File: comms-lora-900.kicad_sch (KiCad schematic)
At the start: 3 parts, among them J3 Conn_Coaxial_Small, U3 RFM95W-915S2

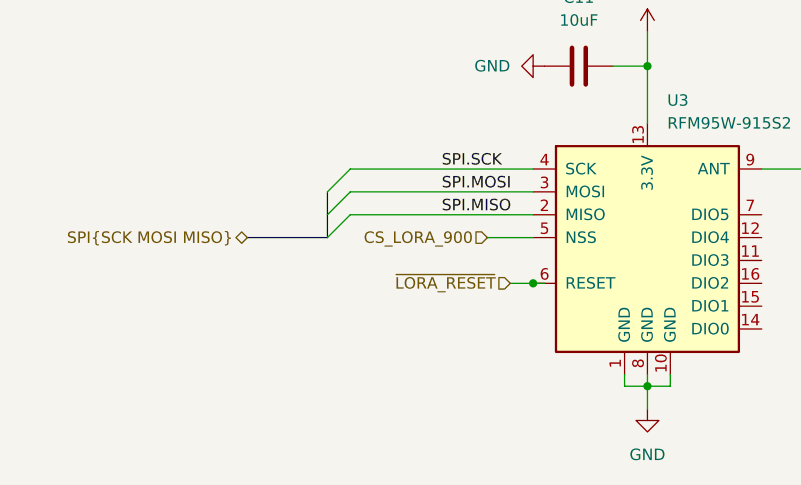
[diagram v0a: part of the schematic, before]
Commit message: Adding symbols information
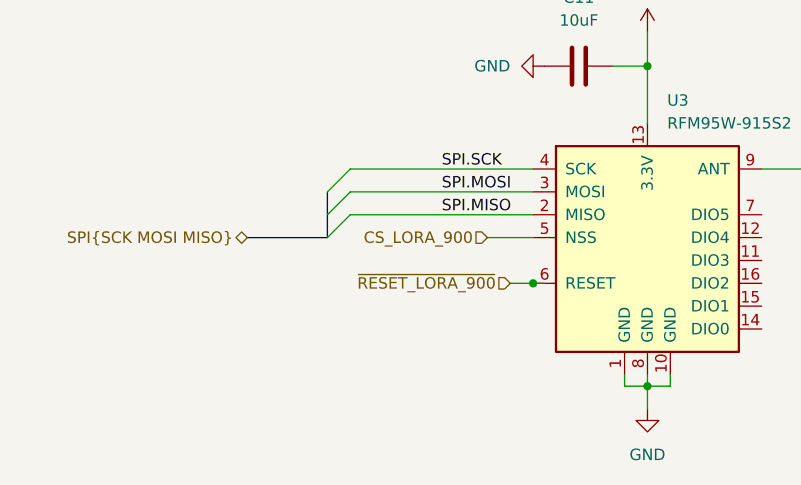
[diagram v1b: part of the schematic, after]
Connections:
- net ~{LORA_RESET} renamed ~{RESET_LORA_900}
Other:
- company: (none) -> catbranchman
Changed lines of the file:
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@@
 	(generator_version "8.0")
 	(paper "A4")
+	(title_block
+		(company "catbranchman")
+		(comment 1 "Electrical Engineering Department")
+		(comment 2 "EE 156 / Stanford University")
+		(comment 3 "Flight Club, W6YX, Endurance")
+	)
 	(junction
 		(at 144.78 114.3)
@@
 		)
 	)
-	(hierarchical_label "~{LORA_RESET}"
+	(hierarchical_label "~{RESET_LORA_900}"
 		(shape input)
 		(at 129.54 102.87 180)
@@
 		)
 		(instances
-			(project ""
+			(project "roamer"
 				(path "/1c59de6a-87fe-4223-8898-4b0383164a31/74b4b058-6b85-4b9e-95dc-72d767f949d9"
 					(reference "J3")
@@
 		)
 		(instances
-			(project ""
+			(project "roamer"
 				(path "/1c59de6a-87fe-4223-8898-4b0383164a31/74b4b058-6b85-4b9e-95dc-72d767f949d9"
 					(reference "C11")

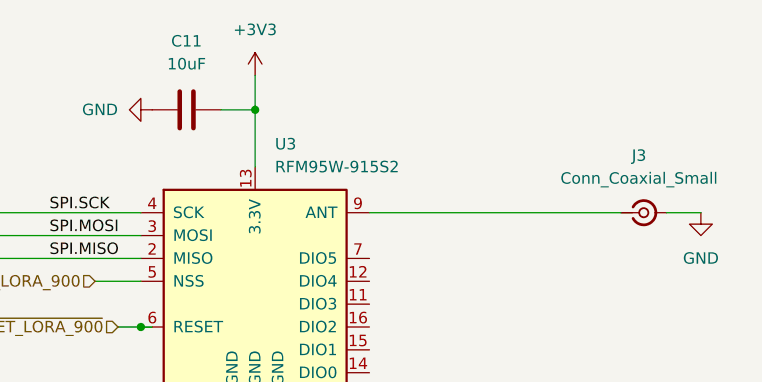
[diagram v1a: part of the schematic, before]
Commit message: Adding rest of schematic
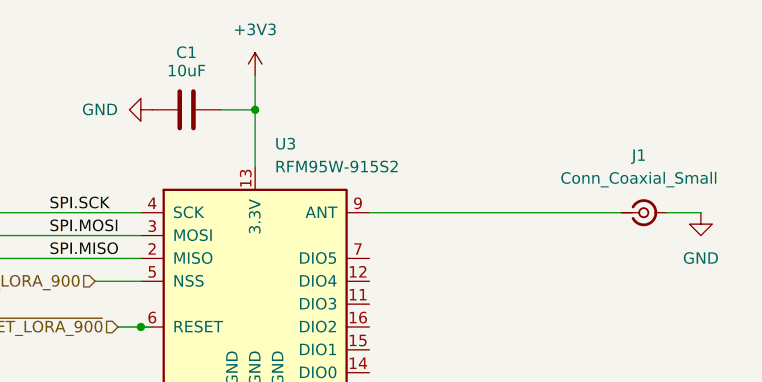
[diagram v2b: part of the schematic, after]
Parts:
- removed C11: 10uF, symbol Device:C
- removed J3: Conn_Coaxial_Small, symbol Connector:Conn_Coaxial_Small
- added C1: 10uF, Inductor_SMD:L_0805_2012Metric, symbol Device:C
- added J1: Conn_Coaxial_Small, Connector_Coaxial:U.FL_Molex_MCRF_73412-0110_Vertical, symbol Connector:Conn_Coaxial_Small
- U3: footprint (none) -> RF_Module:HOPERF_RFM9XW_SMD; Mfr (none) -> Adafruit; Mfr P/N (none) -> 3072; Supplier_1 (none) -> Supplier_1 P/N 0 0 Center Center 0 0; Supplier_1 P/N (none) -> 3072; Supplier_1 Price @ Qty (none) -> $15.96; Supplier_1 Unit Price (none) -> $19.95
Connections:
- net +3V3: now also C1.2
- net GND: now also C1.1, J1.2 (Ext)
- net at U3.9 (ANT): now also J1.1 (In)

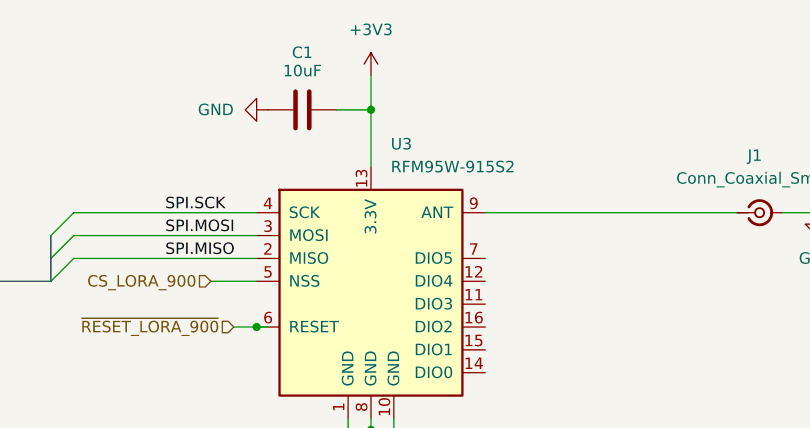
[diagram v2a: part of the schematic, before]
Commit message: Fixing footprint imports
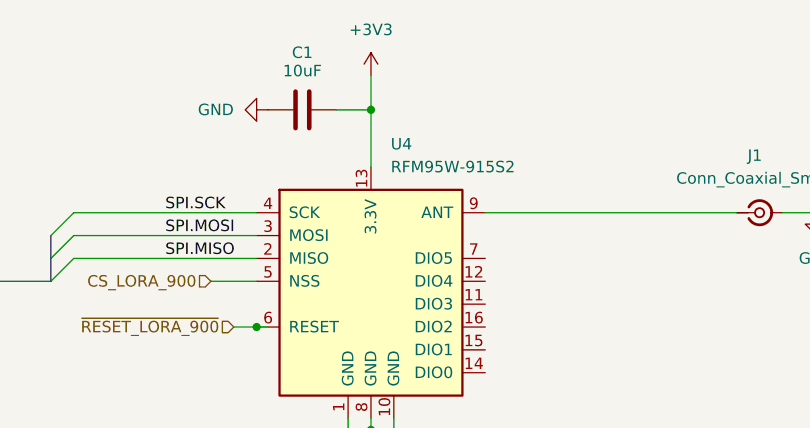
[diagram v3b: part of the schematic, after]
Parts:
- renumbered U3 to U4
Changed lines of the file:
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@@
 		(dnp no)
 		(fields_autoplaced yes)
-		(property "Reference" "U3"
+		(property "Reference" "U4"
 			(at 146.9741 82.55 0)
 			(effects
@@
 			(project "roamer"
 				(path "/1c59de6a-87fe-4223-8898-4b0383164a31/74b4b058-6b85-4b9e-95dc-72d767f949d9"
-					(reference "U3")
+					(reference "U4")
 					(unit 1)
 				)

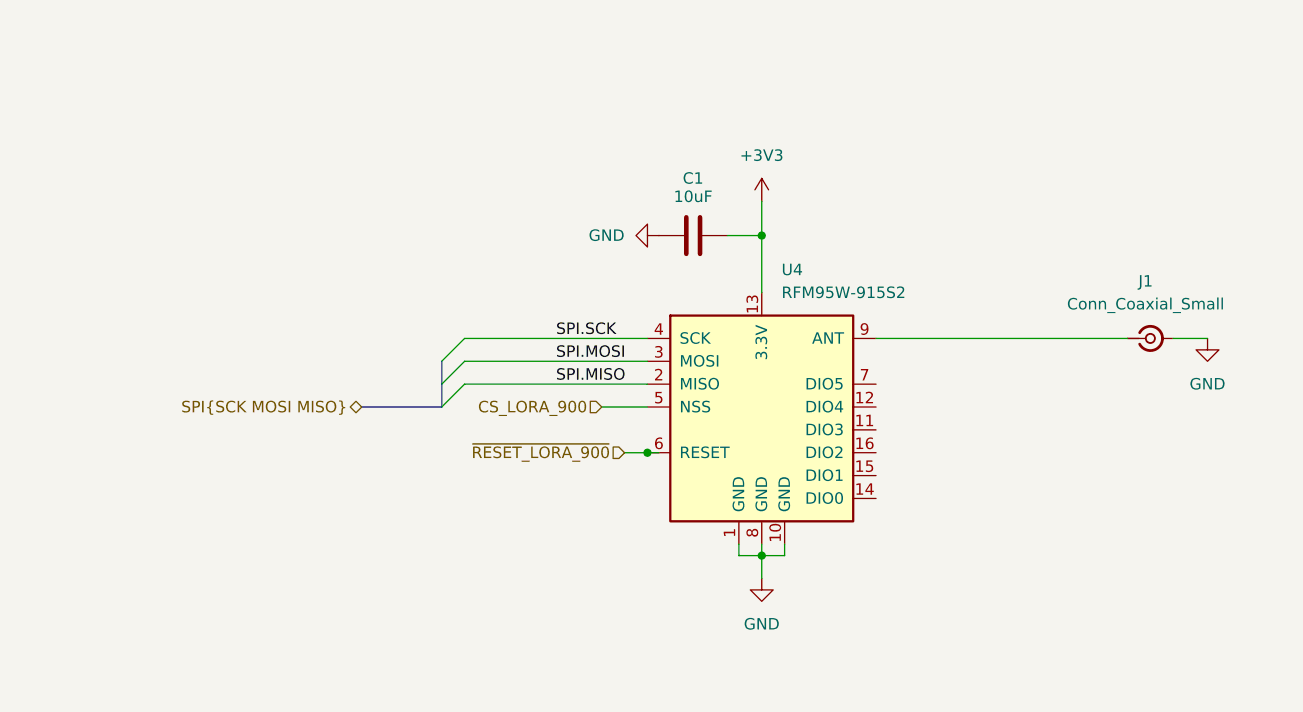
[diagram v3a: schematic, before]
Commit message: Spamming 0 ohm resistors
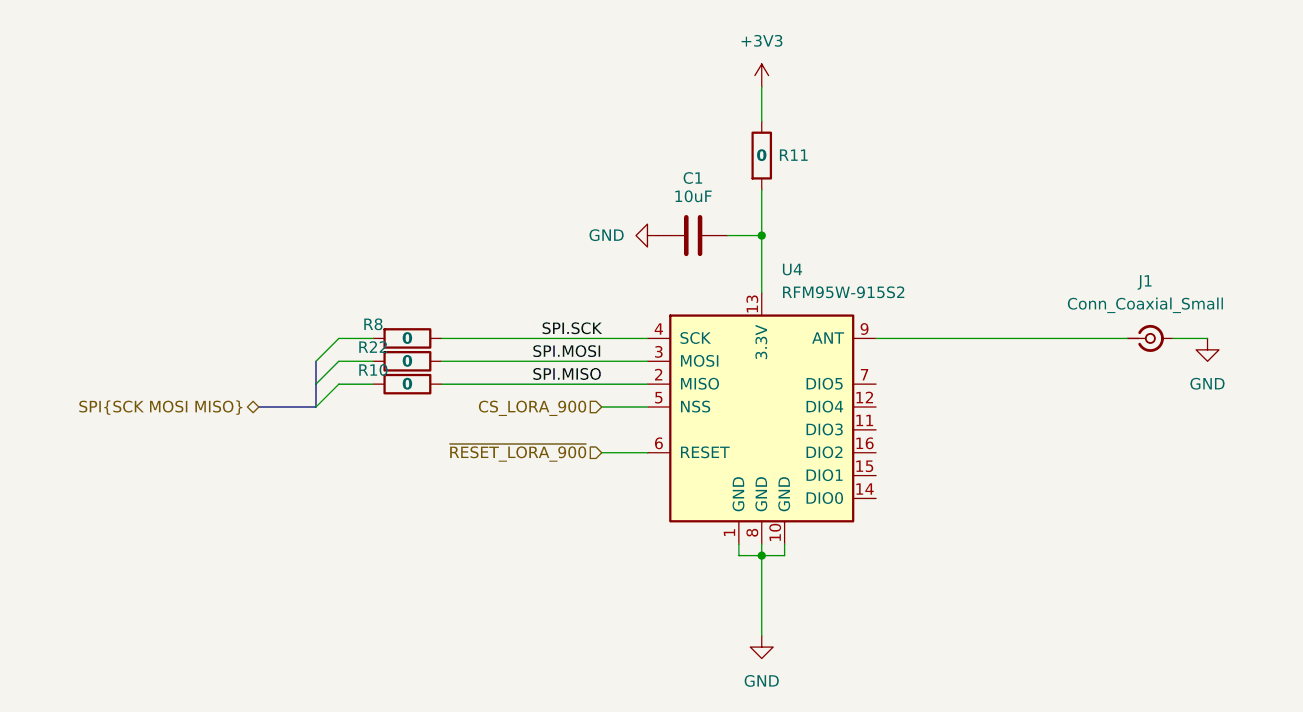
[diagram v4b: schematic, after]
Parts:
- added R10, R11, R22, R8: 0, Resistor_SMD:R_0603_1608Metric, symbol Device:R
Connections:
- net +3V3: now also R11.1; no longer C1.2, U4.13 (3.3V)
- net SPI.MISO: now also R10.1
- net SPI.MOSI: now also R22.1
- net SPI.SCK: now also R8.1
- new net: C1.2, R11.2, U4.13 (3.3V)
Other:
- title: (none) -> Comms - LoRa 900

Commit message: Adding more 0 ohm resistors and pullups for I2C lines
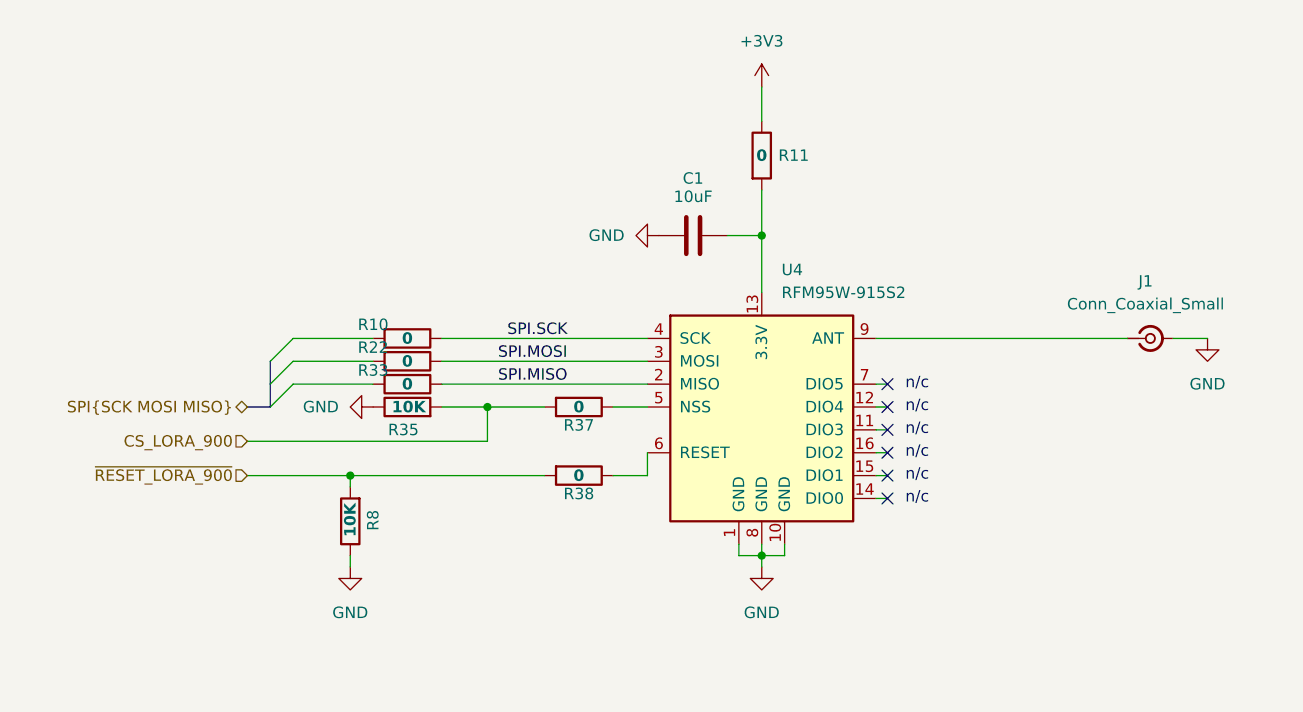
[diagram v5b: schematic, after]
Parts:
- added R33, R37, R38: 0, Resistor_SMD:R_0603_1608Metric, symbol Device:R
- added R35: 10K, Resistor_SMD:R_0603_1608Metric, symbol Device:R
- R8: value 0 -> 10K; Mfr YAGEO -> Stackpole Electronics Inc; Mfr P/N RC0603JR-070RL -> RNCP0603FTD10K0; Supplier_1 P/N 311-0.0GRCT-ND -> RNCP0603FTD10K0CT-ND; Supplier_1 Price @ Qty $0.00304 -> 0.0170; Supplier_1 Unit Price $0.10000 -> 0.10
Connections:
- net CS_LORA_900: now also R35.2, R37.2; no longer U4.5 (NSS)
- net GND: now also R8.1, R35.1
- net SPI.MISO: now also R33.1; no longer R10.1
- net SPI.SCK: now also R10.1; no longer R8.1
- net ~{RESET_LORA_900}: now also R8.2, R38.2; no longer U4.6 (RESET)
- new net: R38.1, U4.6 (RESET)
- new net: R37.1, U4.5 (NSS)
- no-connect marks 0 -> 6
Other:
- note added: "n/c"

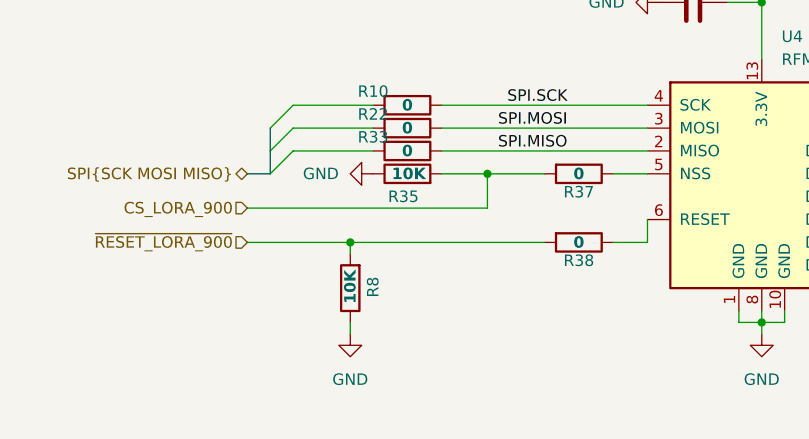
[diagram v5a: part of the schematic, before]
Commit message: Adding testpoints to I2C, SPI, and signals
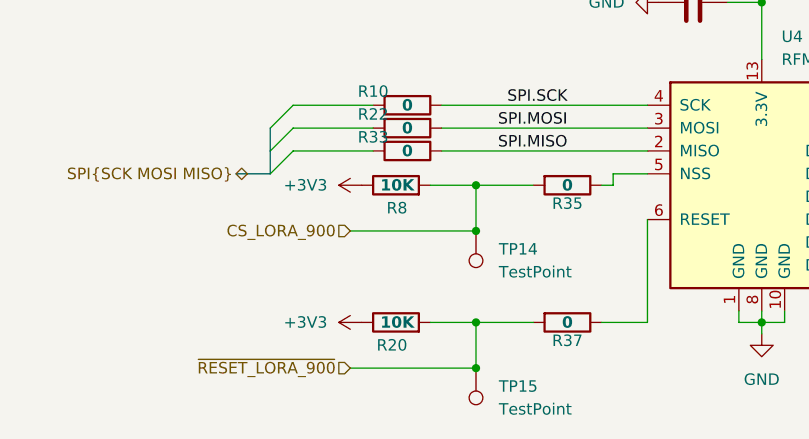
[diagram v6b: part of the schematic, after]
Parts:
- removed R38: 0, Resistor_SMD:R_0603_1608Metric, symbol Device:R
- added R20: 10K, Resistor_SMD:R_0603_1608Metric, symbol Device:R
- added TP14, TP15: TestPoint, TestPoint:TestPoint_Loop_D2.50mm_Drill1.0mm, symbol Connector:TestPoint
- R35: value 10K -> 0; Mfr Stackpole Electronics Inc -> YAGEO; Mfr P/N RNCP0603FTD10K0 -> RC0603JR-070RL; Supplier_1 P/N RNCP0603FTD10K0CT-ND -> 311-0.0GRCT-ND; Supplier_1 Price @ Qty 0.0170 -> $0.00304; Supplier_1 Unit Price 0.10 -> $0.10000
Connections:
- net +3V3: now also R8.1, R20.1
- net CS_LORA_900: now also R8.2, TP14.1; no longer R37.2
- net GND: no longer R35.1, R8.1
- net ~{RESET_LORA_900}: now also R37.2, R20.2, TP15.1; no longer R8.2
- net at U4.6 (RESET): now also R37.1
- net at U4.5 (NSS): now also R35.1; no longer R37.1

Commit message: Fixing lots of ERC errors
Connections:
- net SPI.MISO: now also R33.2; no longer R33.1, U4.2 (MISO)
- net SPI.MOSI: now also R22.2; no longer R22.1, U4.3 (MOSI)
- net SPI.SCK: now also R10.2; no longer R10.1, U4.4 (SCK)
- new net: R10.1, U4.4 (SCK)
- new net: R33.1, U4.2 (MISO)
- new net: R22.1, U4.3 (MOSI)
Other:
- moved on the sheet: C1, R10, R11, R22, R33

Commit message: Redid board layout. Still have to add bypass caps
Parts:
- removed TP14, TP15: TestPoint, TestPoint:TestPoint_Loop_D2.50mm_Drill1.0mm, symbol Connector:TestPoint
